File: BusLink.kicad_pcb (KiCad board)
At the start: 4 copper layers, 4 parts, among them J1 DE9_Pins, J2 USB_C_Receptacle_USB2.0_14P, U1 STM32H723VETx, U2 USB3300-EZK

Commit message: working on power supplies and CAN
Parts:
- removed U2: USB3300-EZK, Package_DFN_QFN:QFN-32-1EP_5x5mm_P0.5mm_EP3.45x3.45mm
- added C1: 1u, Capacitor_SMD:C_0603_1608Metric, F.Cu at (160.1, 110.2)
- added C2: 100n, Capacitor_SMD:C_0603_1608Metric, F.Cu at (160.1, 112.7)
- added C3: 1u, Capacitor_SMD:C_0603_1608Metric, F.Cu at (160.1, 115.2)
- added C4: 100n, Capacitor_SMD:C_0603_1608Metric, F.Cu at (160.1, 117.7)
- added U3: SN65HVD230, Package_SO:SOIC-8_3.9x4.9mm_P1.27mm, F.Cu at (153.9, 112.3)
- added U4: SN65HVD230, Package_SO:SOIC-8_3.9x4.9mm_P1.27mm, F.Cu at (153.9, 118.8)
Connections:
- net Net-(J2-VBUS-PadA4) renamed /USB/5V
- J1 pad 2: /CAN0_LO -> GND
- J1 pad 7: /CAN0_HI -> GND
- J2 pad A1: Net-(J2-GND-PadA1) -> GND
- J2 pad A12: Net-(J2-GND-PadA1) -> GND
- J2 pad A6: unconnected-(J2-D+-PadA6) -> /USB/D+
- J2 pad A7: unconnected-(J2-D--PadA7) -> /USB/D-
- J2 pad B1: Net-(J2-GND-PadA1) -> GND
- J2 pad B12: Net-(J2-GND-PadA1) -> GND
- J2 pad B6: unconnected-(J2-D+-PadB6) -> /USB/D+
- J2 pad B7: unconnected-(J2-D--PadB7) -> /USB/D-
- J2 pad S1: unconnected-(J2-SHIELD-PadS1) -> GND

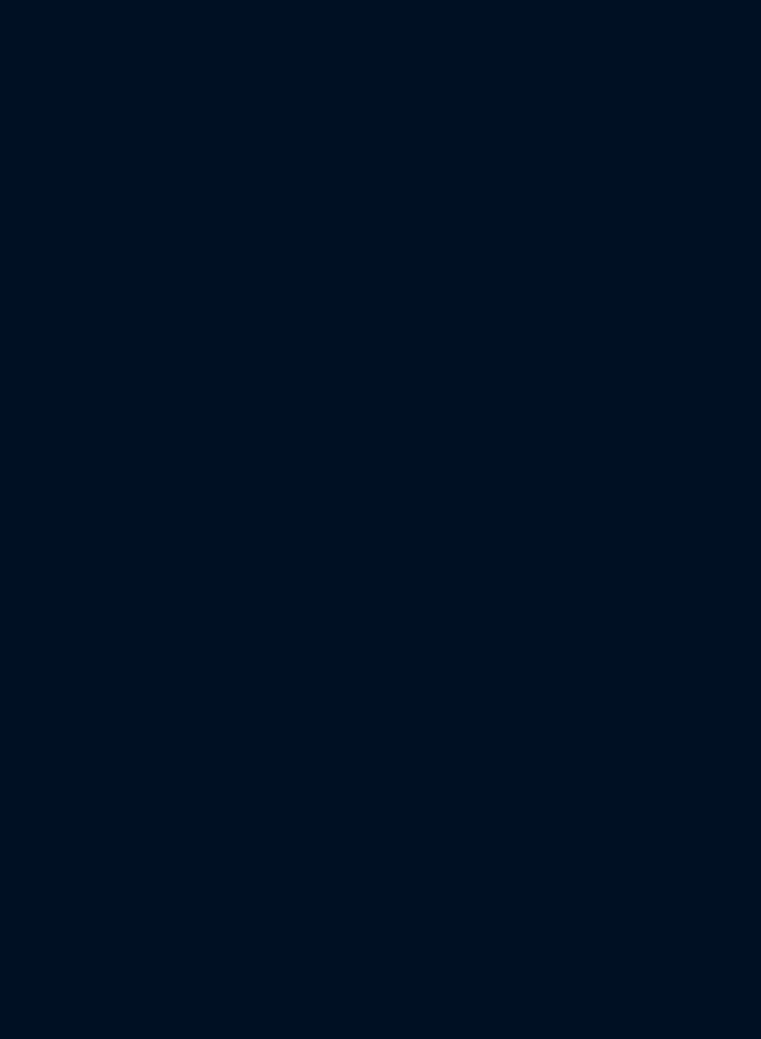
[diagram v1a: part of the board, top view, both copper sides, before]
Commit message: added inductor selection
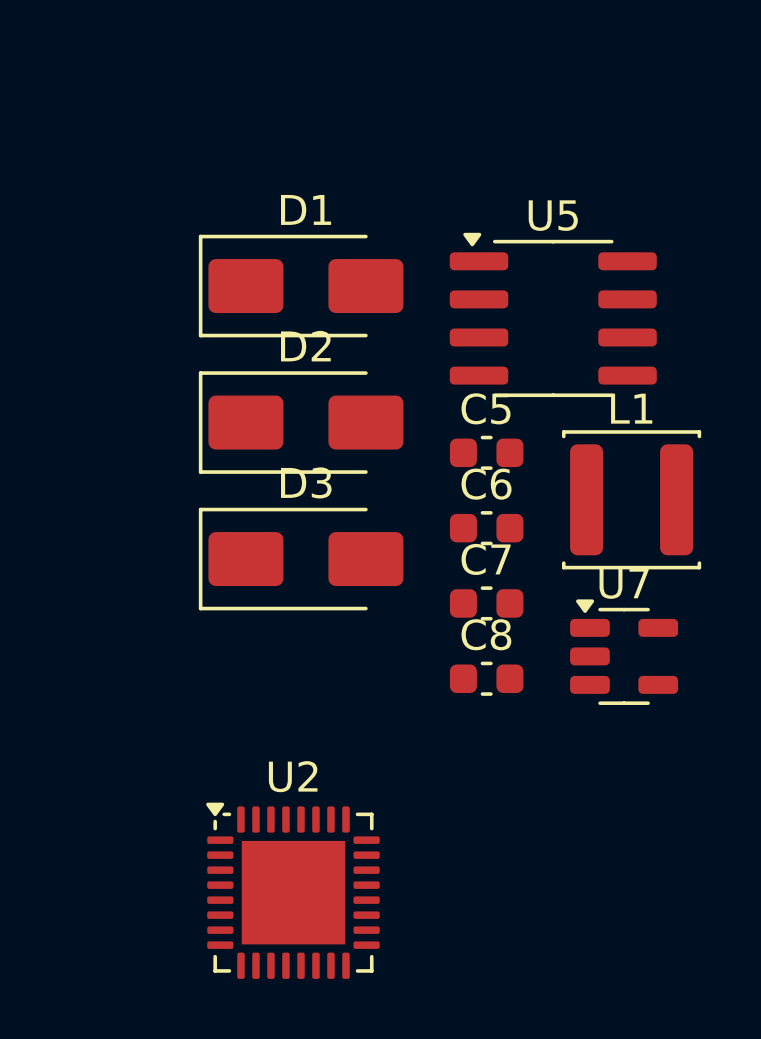
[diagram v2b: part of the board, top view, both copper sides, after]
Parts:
- added C5: 220uF, Capacitor_SMD:C_0603_1608Metric, F.Cu at (183.3, 123.3)
- added C6: 470uF, Capacitor_SMD:C_0603_1608Metric, F.Cu at (183.3, 125.8)
- added C7: 1uF, Capacitor_SMD:C_0603_1608Metric, F.Cu at (183.3, 128.3)
- added C8: 1uF, Capacitor_SMD:C_0603_1608Metric, F.Cu at (183.3, 130.8)
- added D1: SS14, Diode_SMD:D_SMA, F.Cu at (177.3, 117.7)
- added D2: SS14, Diode_SMD:D_SMA, F.Cu at (177.3, 122.3)
- added D3: SS14, Diode_SMD:D_SMA, F.Cu at (177.3, 126.8)
- added L1: 47uH, Inductor_SMD:L_Sunlord_SWPA4030S, F.Cu at (188.1, 124.8)
- added U2: USB3300-EZK, Package_DFN_QFN:QFN-32-1EP_5x5mm_P0.5mm_EP3.45x3.45mm, F.Cu at (176.8, 137.9)
- added U5: XL1509-3.3, Package_SO:SOIC-8_3.9x4.9mm_P1.27mm, F.Cu at (185.5, 118.8)
- added U7: AP2112K-1.8, Package_TO_SOT_SMD:SOT-23-5, F.Cu at (187.9, 130.1)
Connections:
- J1 pad 2: GND -> /CAN0_LO
- J1 pad 7: GND -> /CAN0_HI
- J2 pad A4: /USB/5V -> +5V
- J2 pad A9: /USB/5V -> +5V
- J2 pad B4: /USB/5V -> +5V
- J2 pad B9: /USB/5V -> +5V
- U3 pad 6: GND -> /CAN0_LO
- U3 pad 7: GND -> /CAN0_HI
